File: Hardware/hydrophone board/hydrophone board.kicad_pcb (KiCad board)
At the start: 2 copper layers, 159 parts, among them J1 AudioJack3_Ground, J111 Conn_01x02, J121 Conn_01x02, J131 Conn_01x02, J141 Conn_01x02, J2 AudioJack3_Ground, J211 Conn_01x02, J221 Conn_01x02, J231 Conn_01x02, J241 Conn_01x02, J3 AudioJack3_Ground, J4 AudioJack3_Ground, J401 Conn_01x07, J5 Conn_01x02, J6 Conn_01x02, J7 Conn_01x02, J8 Conn_01x02, U111 AD8541ARTZ, U121 AD8541ARTZ, U131 AD8541ARTZ, U141 AD8541ARTZ, U211 AD8648ARZ, U221 AD8648ARZ, U231 AD8648ARZ, U241 AD8648ARZ, U301 XLV320ADC5140IRTWR, U401 DEV-16771, U501 LT1963AxST-3.3

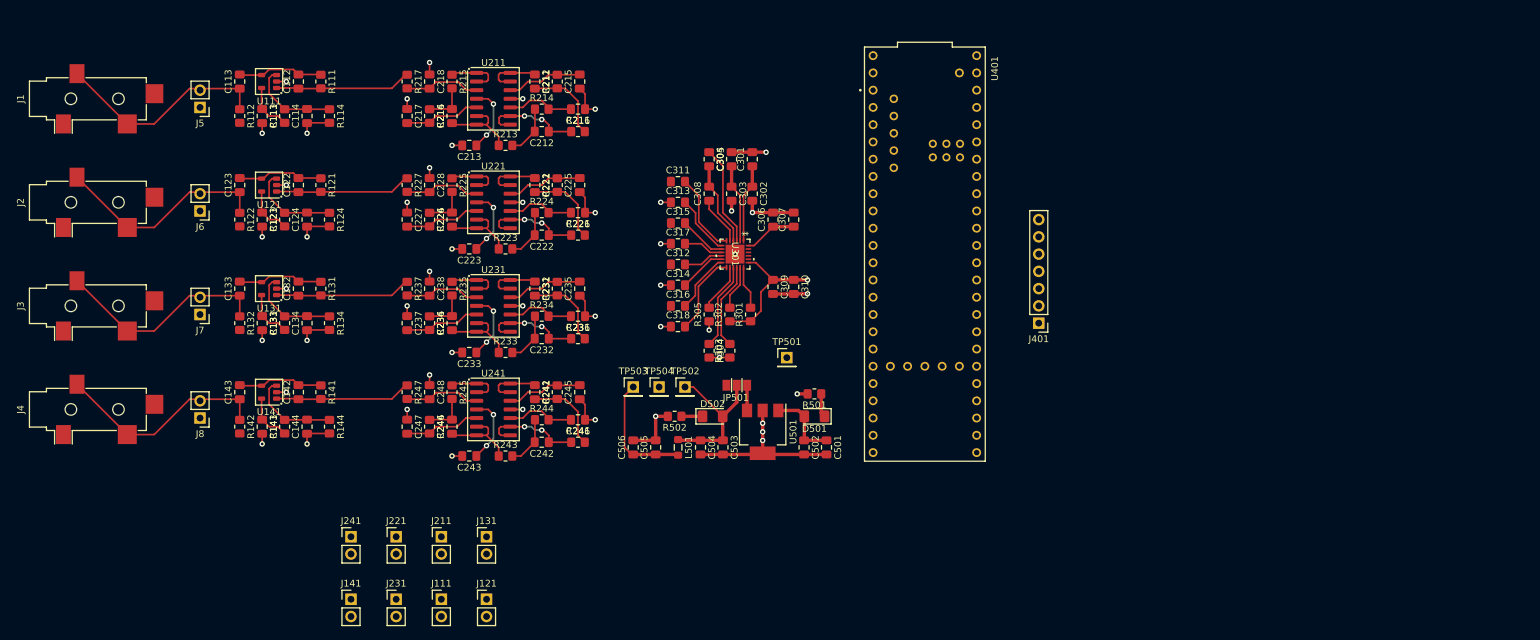
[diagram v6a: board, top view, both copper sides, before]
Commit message: power routing, changed bias voltage to 3.3
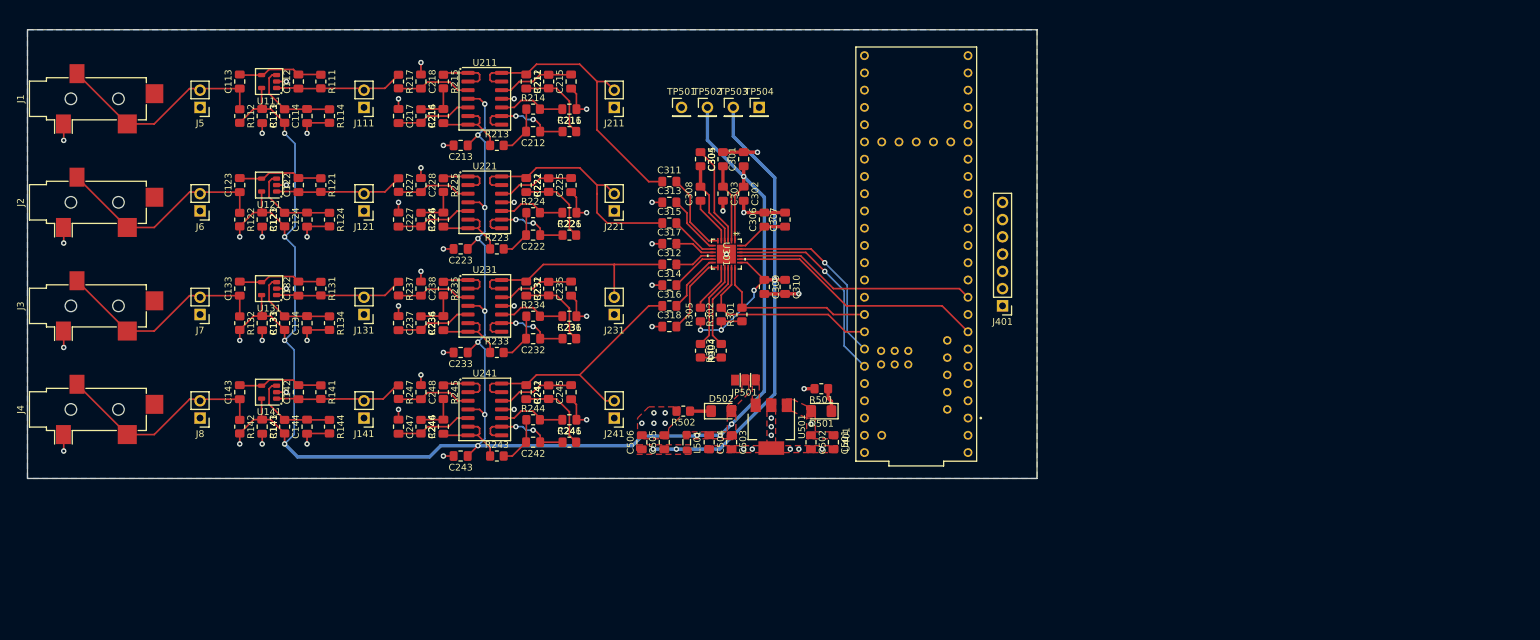
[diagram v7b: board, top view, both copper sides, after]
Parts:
- moved J111 73.3 mm to (113.0, 47.0), turned to 180 degrees
- moved J211 68.1 mm to (149.9, 47.0), turned to 180 degrees
- moved J121 59.9 mm to (113.0, 62.2), turned to 180 degrees
- moved J221 57.7 mm to (149.9, 62.2), turned to 180 degrees
- moved J231 52.8 mm to (149.9, 77.5), turned to 180 degrees
- moved TP503 43.7 mm to (167.4, 47.0)
- moved TP504 43.7 mm to (171.2, 47.0)
- moved J241 42.5 mm to (149.9, 92.7), turned to 180 degrees
- moved TP502 41.3 mm to (163.6, 47.0)
- moved TP501 40.0 mm to (159.8, 47.0)
- moved J131 37.4 mm to (113.0, 77.5), turned to 180 degrees
- moved J141 26.7 mm to (113.0, 92.7), turned to 180 degrees
- moved J401 5.91 mm to (207.0, 76.2)
- moved C503 1.48 mm to (167.1, 96.3)
- moved C504 1.48 mm to (163.8, 96.3)
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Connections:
- R112 pad 2: +5V -> +3.3VA
- R122 pad 2: +5V -> +3.3VA
- R132 pad 2: +5V -> +3.3VA
- R142 pad 2: +5V -> +3.3VA
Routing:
- net +3.3VA: track 103.3 -> 311.3 mm, vias 8 -> 19
- net +3.3VD: track 39.3 -> 92.5 mm, vias 2 -> 6
- net /adc/SDOUT_2: track 0.00 -> 38.0 mm
- net /adc/SDOUT: track 0.00 -> 36.1 mm
- net /IN_1_B: track 8.15 -> 43.2 mm
- net /IN_4_B: track 8.15 -> 39.7 mm
- net /adc/BCLK: track 0.00 -> 30.1 mm, vias 0 -> 1
- net /IN_2_B: track 8.15 -> 37.6 mm
- net /adc/FSYNC: track 0.00 -> 28.5 mm, vias 0 -> 1
- net /IN_3_B: track 8.15 -> 34.0 mm
- net GND: track 156.6 -> 132.7 mm, vias 47 -> 60
- net /adc/SCL: track 6.55 -> 29.1 mm
- net /adc/SDA: track 6.35 -> 24.8 mm
- net +5V: track 11.5 -> 0.56 mm, vias 0 -> 1
- net Net-(JP501-A): track 3.71 -> 0.02 mm
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- added copper zone on F.Cu, net +3.3VA
- added copper zone on F.Cu, net +3.3VD
- added copper zone on F.Cu, net +5V
- added copper zone on B.Cu, net GND
- added copper zone on F.Cu, net GND
- added copper zone on F.Cu, net Net-(JP501-A)
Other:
- board outline added: 148.6 x 66 mm

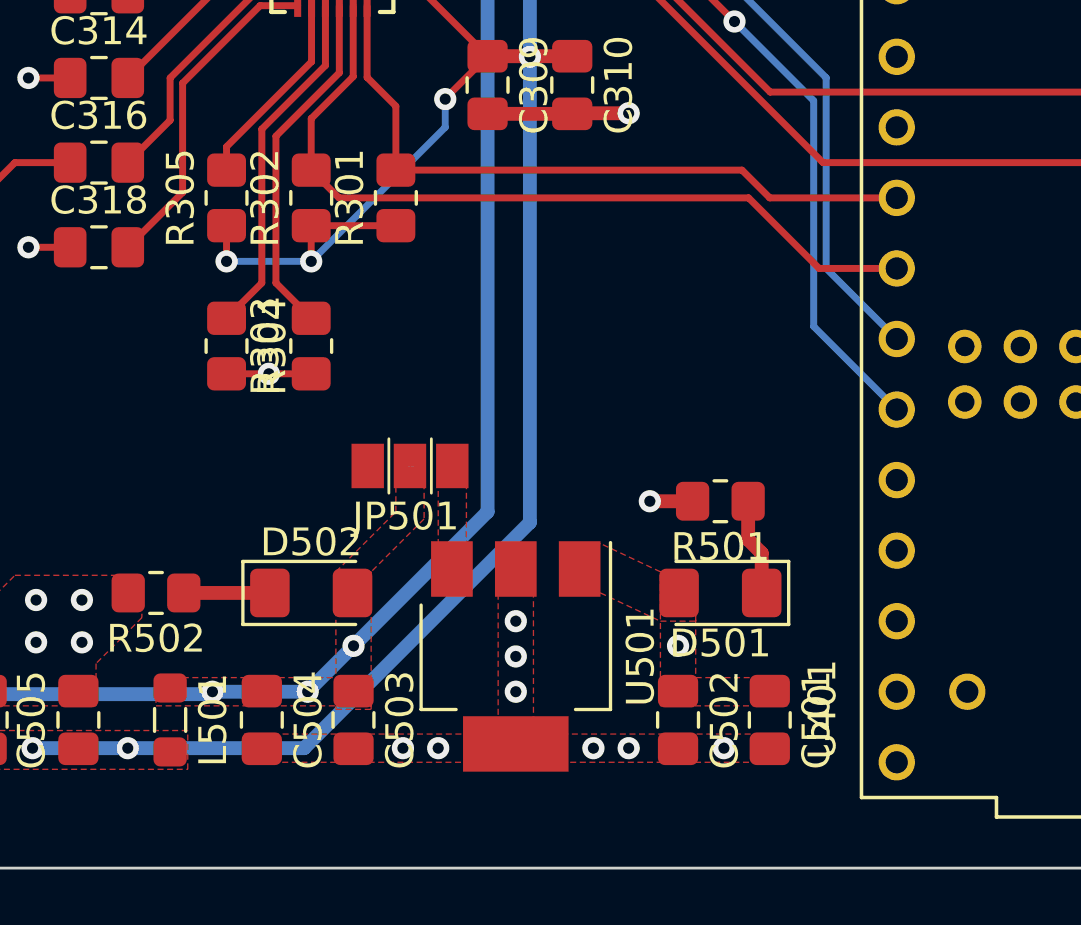
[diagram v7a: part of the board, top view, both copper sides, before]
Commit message: changed 5V pin
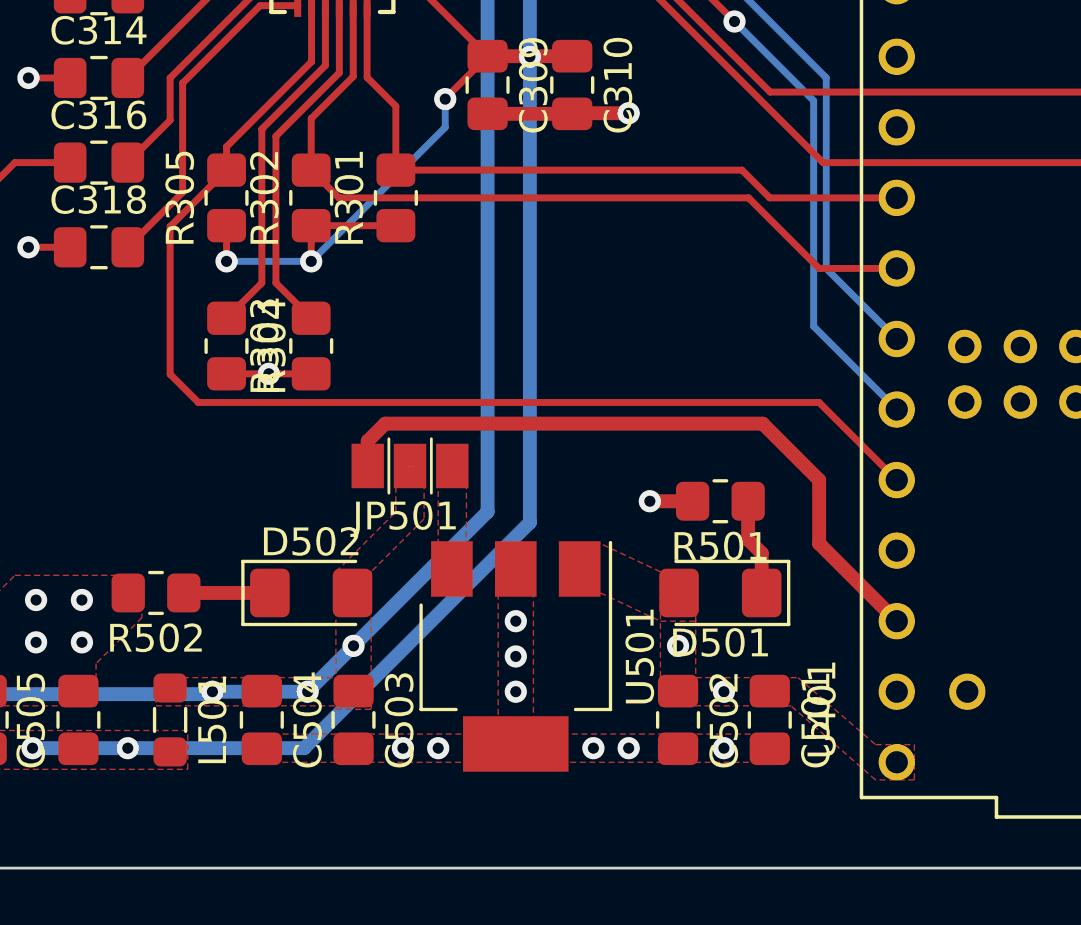
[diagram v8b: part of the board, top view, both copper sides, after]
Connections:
- U401 pad 22: unconnected-(U401-A8-Pad22) -> /adc/SHDNZ
- U401 pad 5V: +5V -> unconnected-(U401-Pad5V)
- U401 pad VIN: unconnected-(U401-PadVIN) -> +5V
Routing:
- net /adc/SHDNZ: track 7.19 -> 43.1 mm
- net /mcu/3.3V MCU: track 0.00 -> 24.5 mm
- net +5V: vias 1 -> 2
